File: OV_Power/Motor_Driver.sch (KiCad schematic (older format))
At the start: 22 parts, among them CN1 CONN_HEADER_R_A_2POS_2.5MM, U3 LMC6772AIMX, U4 VNH5019ATR-E

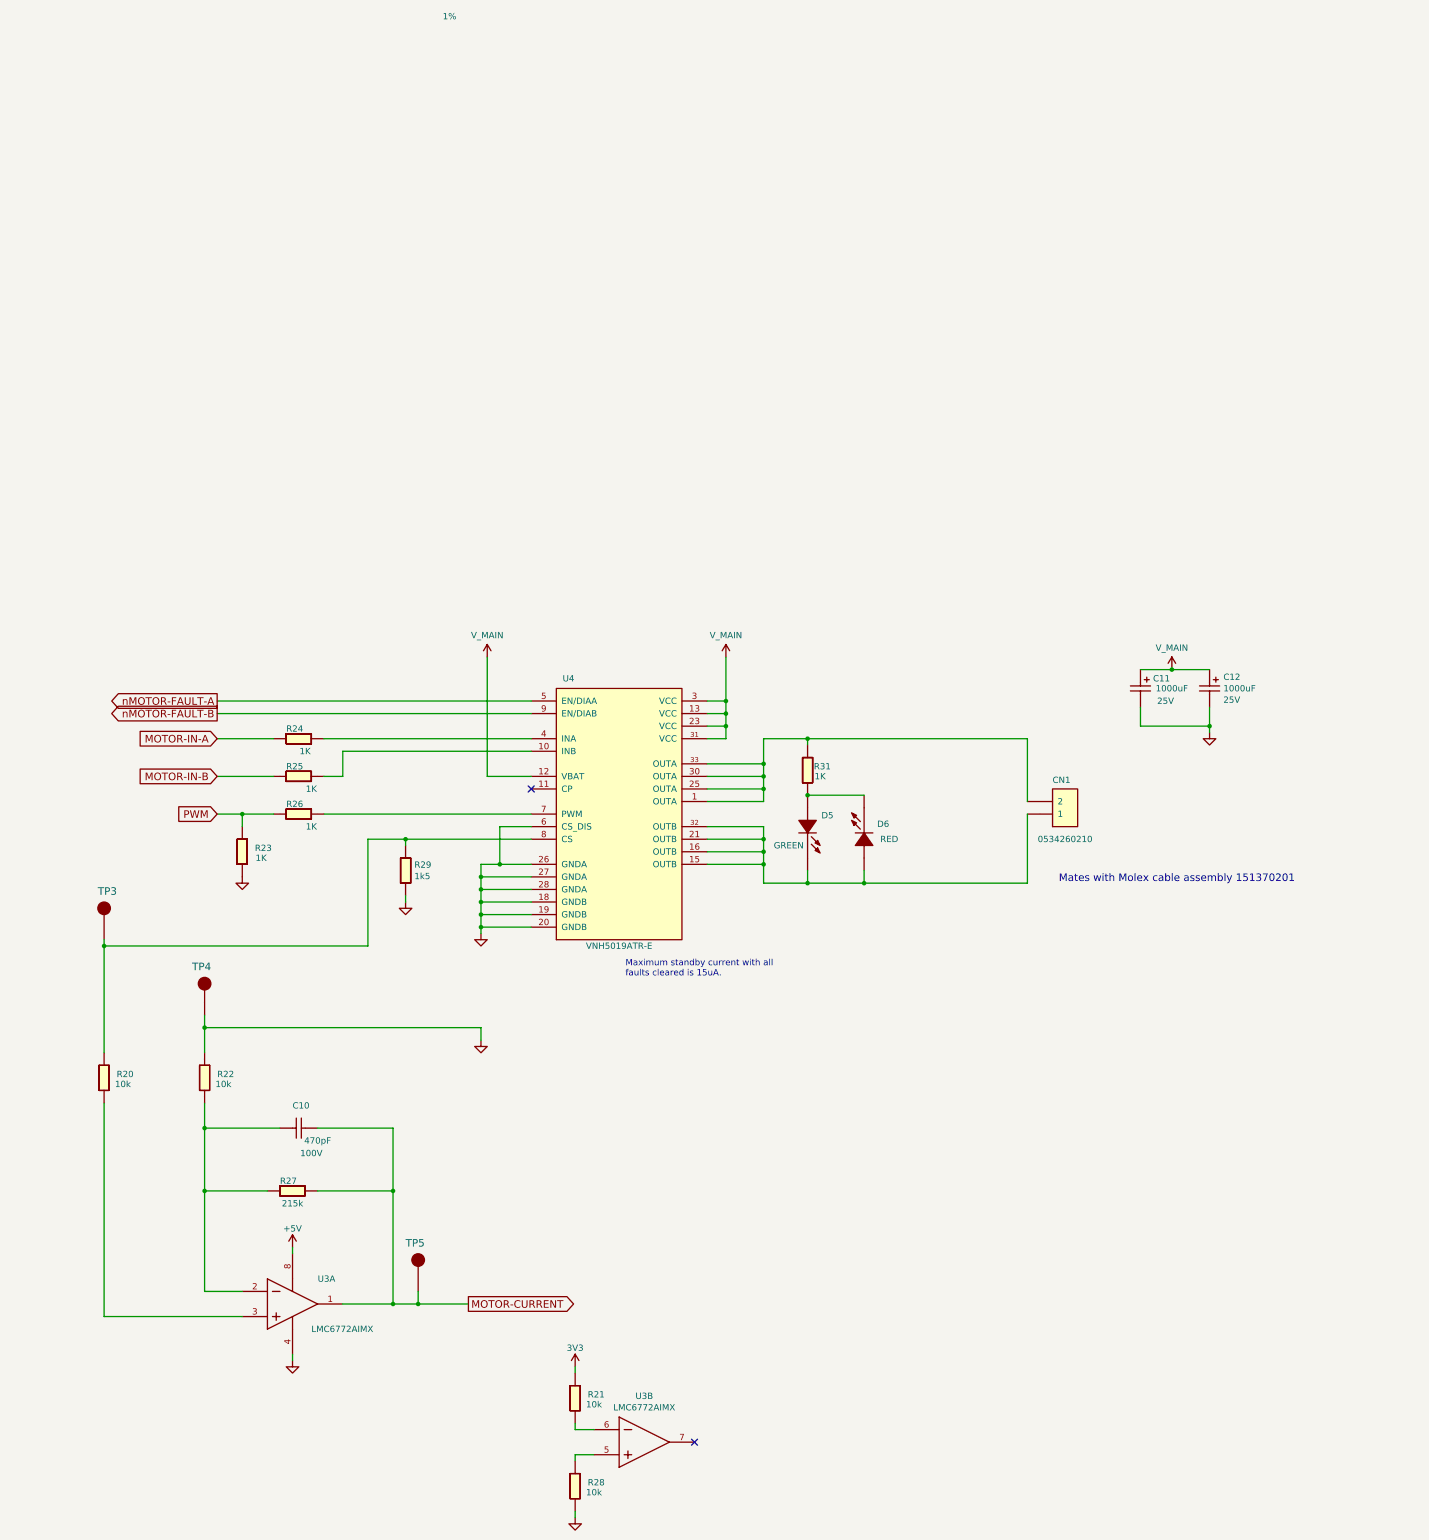
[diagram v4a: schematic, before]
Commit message: Finished schemo and placement of power supply board, then resolved interconnects with the main board.
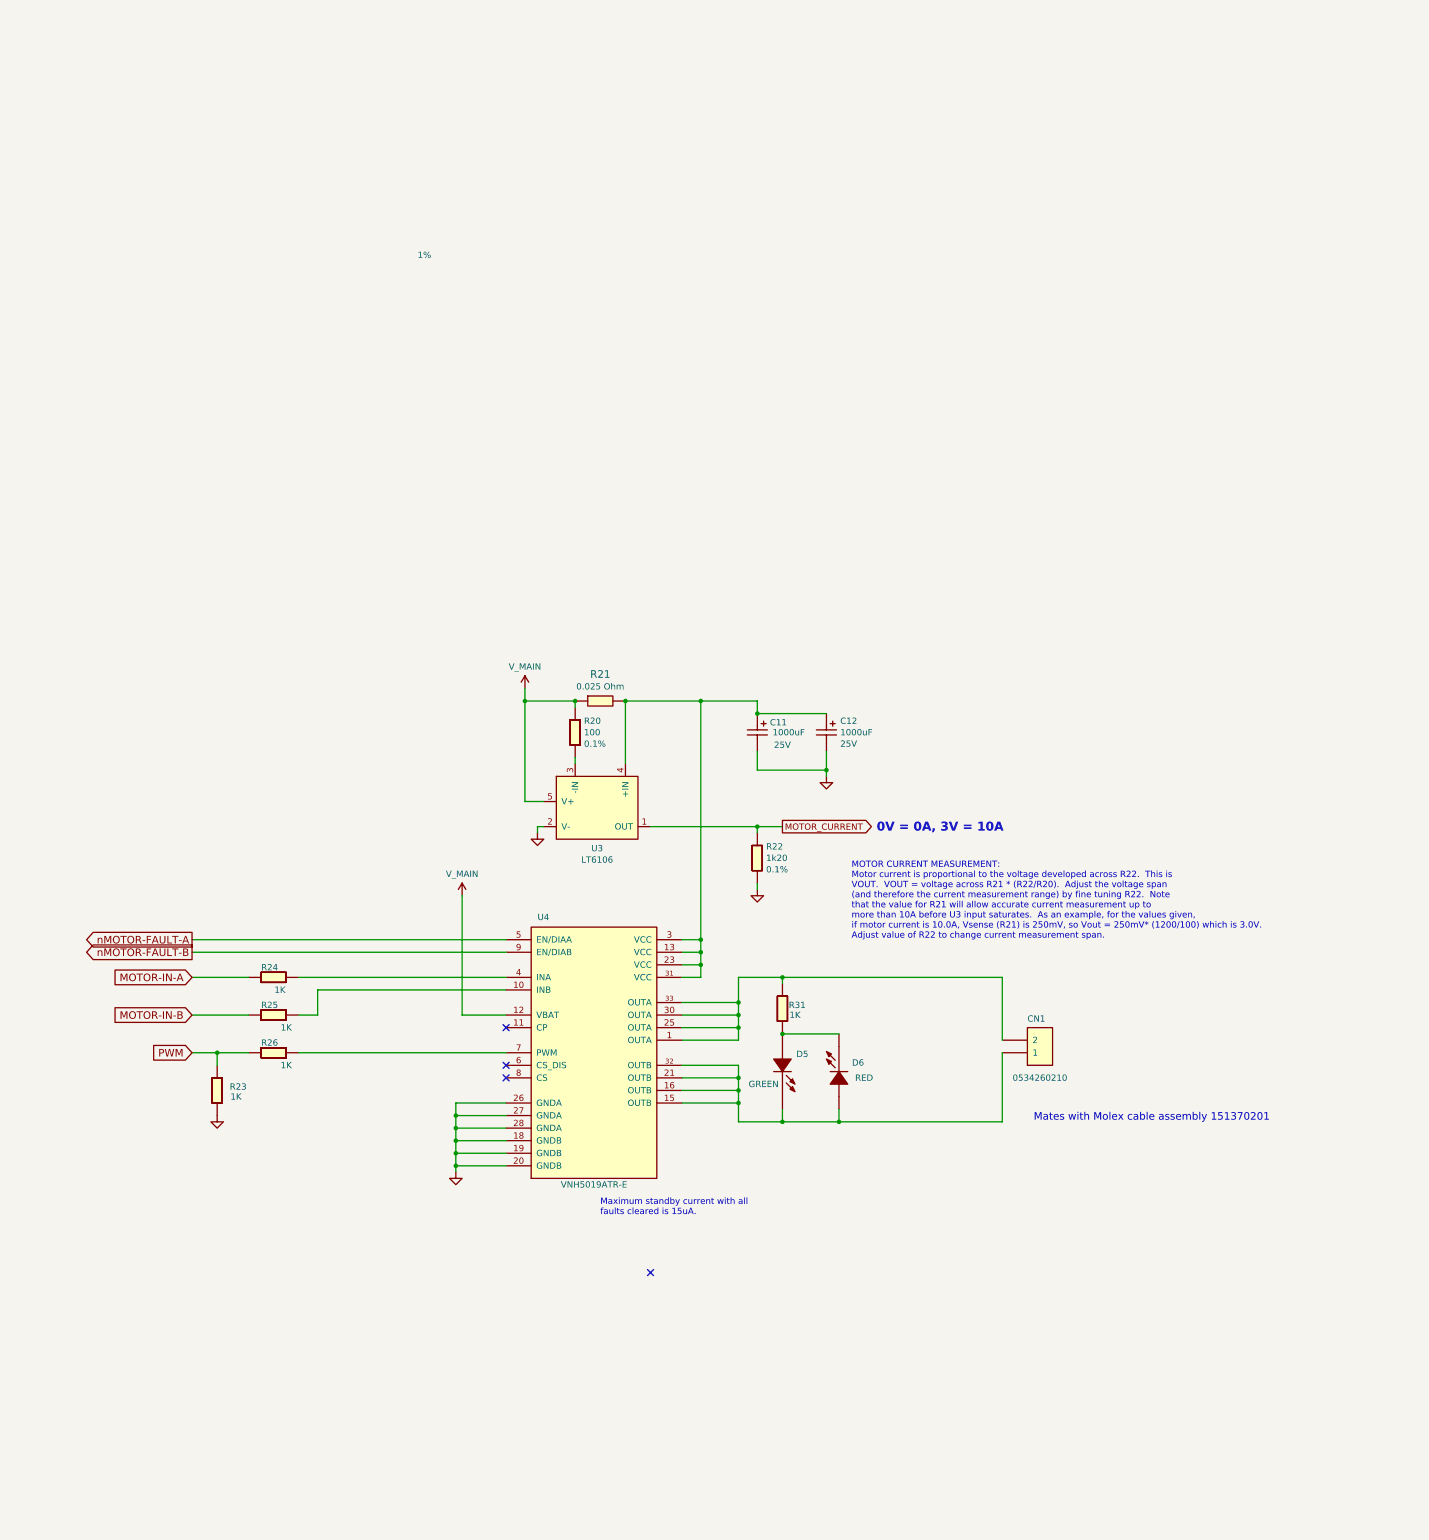
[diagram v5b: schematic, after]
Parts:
- removed C10: 470pF_0603_Ceramic_Capacitor,_5%,_100V,_C0G, Capacitor_SMD:C_0603_1608Metric, symbol OpenVent:470pF_0603_Ceramic_Capacitor,_5%,_100V,_C0G
- removed R20, R21, R22, R28: 10k_0603_Chip_Resistor,_1%,_0.1W, Resistor_SMD:R_0603_1608Metric, symbol OpenVent:10k_0603_Chip_Resistor,_1%,_0.1W
- removed R27: 215k_0603_Chip_Resistor,_1%,_0.1W, Resistor_SMD:R_0603_1608Metric, symbol OpenVent:215k_0603_Chip_Resistor,_1%,_0.1W
- removed R29: R_0603_1k5_0.1W_1%, Resistor_SMD:R_0603_1608Metric, symbol OpenVent:R_0603_1k5_0.1W_1%
- removed TP3, TP4, TP5: Test_Point_PTH, TestPoint:TestPoint_Pad_2.0x2.0mm, symbol OpenVent:Test_Point_PTH
- removed U3: LMC6772AIMX, Package_SO:SO-8_3.9x4.9mm_P1.27mm, symbol OpenVent:LMC6772AIMX
- added R20: R_0603_100_0.1W_0.1%, Resistor_SMD:R_0603_1608Metric, symbol OpenVent:R_0603_100_0.1W_0.1%
- added R21: 0.025 Ohm, Resistor_SMD:R_2010_5025Metric, symbol OpenVent:Resistor_2010_0.025OHM_sensing_1%_1W
- added R22: R_0603_1k2_0.1W_0.1%, Resistor_SMD:R_0603_1608Metric, symbol OpenVent:R_0603_1k2_0.1W_0.1%
- added U3: LT6106, Package_TO_SOT_SMD:TSOT-23-5, symbol F_ICs:LT6106
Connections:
- net GND: now also R22.2, U3.2 (V-); no longer U4.6 (CS_DIS)
- net V_MAIN: now also R20.1, R21.1, U3.5 (V+); no longer C11.1 (+), C12.1 (+), U4.13 (VCC), U4.23 (VCC), U4.3 (VCC), U4.31 (VCC)
- new net: C11.1 (+), C12.1 (+), R21.2, U3.4 (+IN), U4.13 (VCC), U4.23 (VCC), U4.3 (VCC), U4.31 (VCC)
- new net: R20.2, U3.3 (-IN)
- new net MOTOR_CURRENT: R22.1, U3.1 (OUT)
- no-connect marks 2 -> 4
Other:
- note added: "0V = 0A, 3V = 10A"
- note added: "MOTOR CURRENT MEASUREMENT:\nMotor current is proportional to the voltage developed across R22. This is\nVOUT. VOUT = voltage across R21 * (R22/R20). Adjust the voltage span\n(and therefore the current measurement range) by fine tuning R22. Note\nthat the value for R21 will allow accurate current measurement up to\nmore than 10A before U3 input saturates. As an example, for the values given,\nif m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"
- moved on the sheet: C11, C12, CN1, D5, D6, R23, R24, R25, R26, R31, U4
